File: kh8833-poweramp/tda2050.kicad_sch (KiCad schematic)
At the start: 13 parts, among them U1 TDA2050

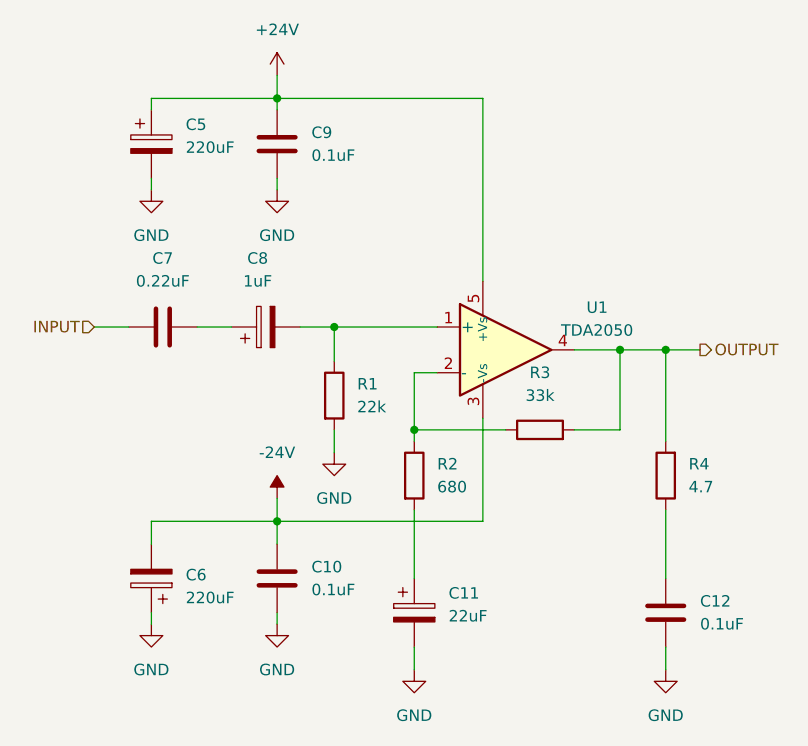
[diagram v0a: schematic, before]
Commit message: Add speaker prot - v1.0
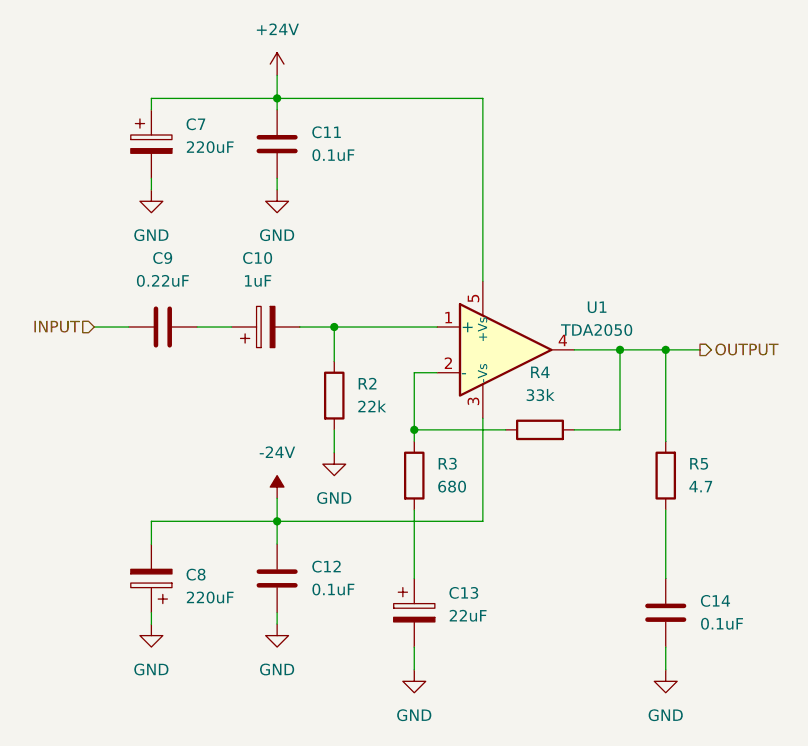
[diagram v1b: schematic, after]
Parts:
- renumbered C8 to C10, C9 to C11, C10 to C12, C11 to C13, C12 to C14, C5 to C7, C6 to C8, C7 to C9, R1 to R2, R2 to R3, R3 to R4, R4 to R5
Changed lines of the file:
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@@
   (symbol (lib_id "power:GND") (at 138.43 106.68 0) (unit 1)
     (in_bom yes) (on_board yes) (fields_autoplaced)
-    (property "Reference" "#PWR019" (id 0) (at 138.43 113.03 0)
+    (property "Reference" "#PWR022" (id 0) (at 138.43 113.03 0)
       (effects (font (size 1.27 1.27)) hide)
     )
@@
   (symbol (lib_id "power:GND") (at 132.08 125.73 0) (unit 1)
     (in_bom yes) (on_board yes) (fields_autoplaced)
-    (property "Reference" "#PWR018" (id 0) (at 132.08 132.08 0)
+    (property "Reference" "#PWR021" (id 0) (at 132.08 132.08 0)
       (effects (font (size 1.27 1.27)) hide)
     )
@@
   (symbol (lib_id "Device:C") (at 119.38 92.71 90) (unit 1)
     (in_bom yes) (on_board yes) (fields_autoplaced)
-    (property "Reference" "C7" (id 0) (at 119.38 85.09 90))
+    (property "Reference" "C9" (id 0) (at 119.38 85.09 90))
     (property "Value" "0.22uF" (id 1) (at 119.38 87.63 90))
     (property "Footprint" "Capacitor_THT:C_Disc_D7.5mm_W5.0mm_P7.50mm" (id 2) (at 123.19 91.7448 0)
@@
   (symbol (lib_id "power:GND") (at 118.11 77.47 0) (unit 1)
     (in_bom yes) (on_board yes) (fields_autoplaced)
-    (property "Reference" "#PWR013" (id 0) (at 118.11 83.82 0)
+    (property "Reference" "#PWR016" (id 0) (at 118.11 83.82 0)
       (effects (font (size 1.27 1.27)) hide)
     )
@@
   (symbol (lib_id "Device:R") (at 147.32 109.22 0) (unit 1)
     (in_bom yes) (on_board yes) (fields_autoplaced)
-    (property "Reference" "R2" (id 0) (at 149.86 107.9499 0)
+    (property "Reference" "R3" (id 0) (at 149.86 107.9499 0)
       (effects (font (size 1.27 1.27)) (justify left))
     )
@@
   (symbol (lib_id "power:GND") (at 175.26 130.81 0) (unit 1)
     (in_bom yes) (on_board yes) (fields_autoplaced)
-    (property "Reference" "#PWR021" (id 0) (at 175.26 137.16 0)
+    (property "Reference" "#PWR024" (id 0) (at 175.26 137.16 0)
       (effects (font (size 1.27 1.27)) hide)
     )
@@
   (symbol (lib_id "Device:C_Polarized") (at 118.11 120.65 180) (unit 1)
     (in_bom yes) (on_board yes) (fields_autoplaced)
-    (property "Reference" "C6" (id 0) (at 121.92 120.2689 0)
+    (property "Reference" "C8" (id 0) (at 121.92 120.2689 0)
       (effects (font (size 1.27 1.27)) (justify right))
     )
@@
   (symbol (lib_id "Device:R") (at 138.43 100.33 0) (unit 1)
     (in_bom yes) (on_board yes) (fields_autoplaced)
-    (property "Reference" "R1" (id 0) (at 140.97 99.0599 0)
+    (property "Reference" "R2" (id 0) (at 140.97 99.0599 0)
       (effects (font (size 1.27 1.27)) (justify left))
     )
@@
   (symbol (lib_id "power:GND") (at 118.11 125.73 0) (unit 1)
     (in_bom yes) (on_board yes) (fields_autoplaced)
-    (property "Reference" "#PWR014" (id 0) (at 118.11 132.08 0)
+    (property "Reference" "#PWR017" (id 0) (at 118.11 132.08 0)
       (effects (font (size 1.27 1.27)) hide)
     )
@@
   (symbol (lib_id "Device:C") (at 132.08 120.65 0) (unit 1)
     (in_bom yes) (on_board yes) (fields_autoplaced)
-    (property "Reference" "C10" (id 0) (at 135.89 119.3799 0)
+    (property "Reference" "C12" (id 0) (at 135.89 119.3799 0)
       (effects (font (size 1.27 1.27)) (justify left))
     )
@@
   (symbol (lib_id "Device:R") (at 175.26 109.22 180) (unit 1)
     (in_bom yes) (on_board yes) (fields_autoplaced)
-    (property "Reference" "R4" (id 0) (at 177.8 107.9499 0)
+    (property "Reference" "R5" (id 0) (at 177.8 107.9499 0)
       (effects (font (size 1.27 1.27)) (justify right))
     )
@@
   (symbol (lib_id "power:GND") (at 132.08 77.47 0) (unit 1)
     (in_bom yes) (on_board yes) (fields_autoplaced)
-    (property "Reference" "#PWR016" (id 0) (at 132.08 83.82 0)
+    (property "Reference" "#PWR019" (id 0) (at 132.08 83.82 0)
       (effects (font (size 1.27 1.27)) hide)
     )
@@
   (symbol (lib_id "power:+24V") (at 132.08 64.77 0) (unit 1)
     (in_bom yes) (on_board yes) (fields_autoplaced)
-    (property "Reference" "#PWR015" (id 0) (at 132.08 68.58 0)
+    (property "Reference" "#PWR018" (id 0) (at 132.08 68.58 0)
       (effects (font (size 1.27 1.27)) hide)
     )
@@
   (symbol (lib_id "Device:C") (at 132.08 72.39 0) (unit 1)
     (in_bom yes) (on_board yes) (fields_autoplaced)
-    (property "Reference" "C9" (id 0) (at 135.89 71.1199 0)
+    (property "Reference" "C11" (id 0) (at 135.89 71.1199 0)
       (effects (font (size 1.27 1.27)) (justify left))
     )
@@
   (symbol (lib_id "Device:C_Polarized") (at 118.11 72.39 0) (unit 1)
     (in_bom yes) (on_board yes) (fields_autoplaced)
-    (property "Reference" "C5" (id 0) (at 121.92 70.2309 0)
+    (property "Reference" "C7" (id 0) (at 121.92 70.2309 0)
       (effects (font (size 1.27 1.27)) (justify left))
     )
@@
   (symbol (lib_id "Device:C_Polarized") (at 147.32 124.46 0) (unit 1)
     (in_bom yes) (on_board yes) (fields_autoplaced)
-    (property "Reference" "C11" (id 0) (at 151.13 122.3009 0)
+    (property "Reference" "C13" (id 0) (at 151.13 122.3009 0)
       (effects (font (size 1.27 1.27)) (justify left))
     )
@@
   (symbol (lib_id "power:-24V") (at 132.08 111.76 0) (unit 1)
     (in_bom yes) (on_board yes) (fields_autoplaced)
-    (property "Reference" "#PWR017" (id 0) (at 132.08 109.22 0)
+    (property "Reference" "#PWR020" (id 0) (at 132.08 109.22 0)
       (effects (font (size 1.27 1.27)) hide)
     )
@@
   (symbol (lib_id "Device:C") (at 175.26 124.46 0) (unit 1)
     (in_bom yes) (on_board yes) (fields_autoplaced)
-    (property "Reference" "C12" (id 0) (at 179.07 123.1899 0)
+    (property "Reference" "C14" (id 0) (at 179.07 123.1899 0)
       (effects (font (size 1.27 1.27)) (justify left))
     )
@@
   (symbol (lib_id "Device:C_Polarized") (at 130.81 92.71 90) (unit 1)
     (in_bom yes) (on_board yes) (fields_autoplaced)
-    (property "Reference" "C8" (id 0) (at 129.921 85.09 90))
+    (property "Reference" "C10" (id 0) (at 129.921 85.09 90))
     (property "Value" "1uF" (id 1) (at 129.921 87.63 90))
     (property "Footprint" "Capacitor_THT:CP_Radial_D8.0mm_P5.00mm" (id 2) (at 134.62 91.7448 0)
@@
   (symbol (lib_id "power:GND") (at 147.32 130.81 0) (unit 1)
     (in_bom yes) (on_board yes) (fields_autoplaced)
-    (property "Reference" "#PWR020" (id 0) (at 147.32 137.16 0)
+    (property "Reference" "#PWR023" (id 0) (at 147.32 137.16 0)
       (effects (font (size 1.27 1.27)) hide)
     )
@@
   (symbol (lib_id "Device:R") (at 161.29 104.14 90) (unit 1)
     (in_bom yes) (on_board yes) (fields_autoplaced)
-    (property "Reference" "R3" (id 0) (at 161.29 97.79 90))
+    (property "Reference" "R4" (id 0) (at 161.29 97.79 90))
     (property "Value" "33k" (id 1) (at 161.29 100.33 90))
     (property "Footprint" "Resistor_THT:R_Axial_DIN0207_L6.3mm_D2.5mm_P10.16mm_Horizontal" (id 2) (at 161.29 105.918 90)
